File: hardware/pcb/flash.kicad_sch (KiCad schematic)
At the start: 0 parts

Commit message: Update(hardware): Completed some schematics
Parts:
- added C7: 100n, Package_SON:WSON-8-1EP_6x5mm_P1.27mm_EP3.4x4.3mm, symbol Device:C
- added R1: 10k, Package_SON:WSON-8-1EP_6x5mm_P1.27mm_EP3.4x4.3mm, symbol Device:R
- added R2: 10, symbol Device:R
- added U7: IS25WP256D-JLLE, Package_SON:WSON-8-1EP_6x5mm_P1.27mm_EP3.4x4.3mm, symbol IS25WP256D-JLLE:IS25WP256D-JLLE
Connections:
- net CE# (QSPI CSN): now also R1.1
- net HOLD# (IO3): now also U7.7 (HOLD#/RESET#/IO3)
- net SCK: now also R2.1
- net SI (IO0): now also U7.5 (SI/IO0)
- net SO (IO1): now also U7.2 (SO/IO1)
- net WP# (IO2): now also U7.3 (WP#/IO2)
- new net: R1.2, U7.1 (CE#)
- new net: R2.2, U7.6 (SCK)
- new net +1V8: C7.1, U7.8 (VCC)
- new net GNDPWR: C7.2, U7.4 (GND)
- no-connect marks 0 -> 1
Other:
- note added: "Documentation available here"
- note added: "Operation voltage 1.8V (use a level shifter SPI IO)"

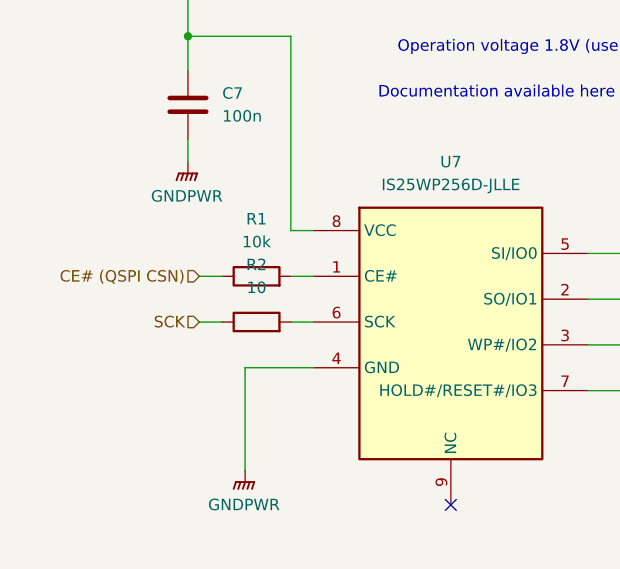
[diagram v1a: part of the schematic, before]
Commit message: Changed GNDPWR to GND and changed GND to speciality GNDs
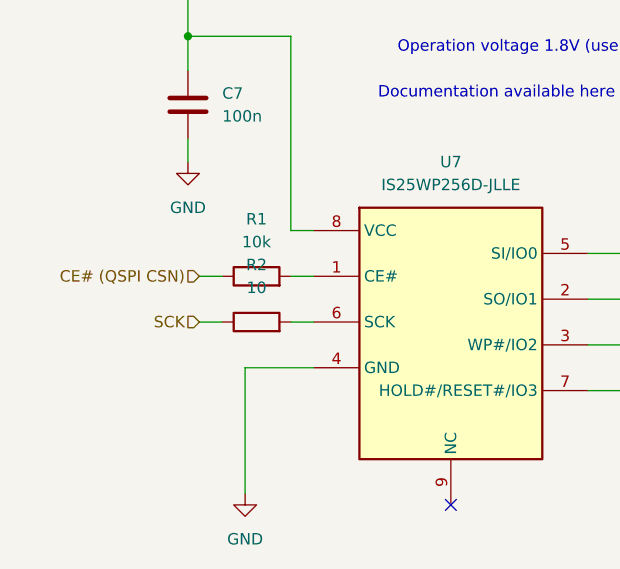
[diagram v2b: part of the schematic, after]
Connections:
- net GNDPWR renamed GND
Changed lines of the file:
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@@
 	(wire
 		(pts
-			(xy 101.6 104.14) (xy 101.6 115.57)
+			(xy 101.6 104.14) (xy 101.6 118.11)
 		)
 		(stroke
@@
 			)
 			(justify right)
-		)
-	)
-	(symbol
-		(lib_id "power:GNDPWR")
-		(at 101.6 115.57 0)
-		(unit 1)
-		(body_style 1)
-		(exclude_from_sim no)
-		(in_bom yes)
-		(on_board yes)
-		(in_pos_files yes)
-		(dnp no)
-		(fields_autoplaced yes)
-		(property "Reference" "#PWR024"
-			(at 101.6 120.65 0)
-			(hide yes)
-			(show_name no)
-			(do_not_autoplace no)
-			(effects
-				(font
-					(size 1.27 1.27)
-				)
-			)
-		)
-		(property "Value" "GNDPWR"
-			(at 101.473 119.38 0)
-			(show_name no)
-			(do_not_autoplace no)
-			(effects
-				(font
-					(size 1.27 1.27)
-				)
-			)
-		)
-		(property "Footprint" ""
-			(at 101.6 116.84 0)
-			(hide yes)
-			(show_name no)
-			(do_not_autoplace no)
-			(effects
-				(font
-					(size 1.27 1.27)
-				)
-			)
-		)
-		(property "Datasheet" ""
-			(at 101.6 116.84 0)
-			(hide yes)
-			(show_name no)
-			(do_not_autoplace no)
-			(effects
-				(font
-					(size 1.27 1.27)
-				)
-			)
-		)
-		(property "Description" "Power symbol creates a global label with name \"GNDPWR\" , global ground"
-			(at 101.6 115.57 0)
-			(hide yes)
-			(show_name no)
-			(do_not_autoplace no)
-			(effects
-				(font
-					(size 1.27 1.27)
-				)
-			)
-		)
-		(pin "1"
-		)
-		(instances
-			(project "test-circuits"
-				(path "/7b1b7b91-6618-446c-b915-39ecd9748633/cf3b1c17-62ba-4998-8a74-365c3fc0ceaf"
-					(reference "#PWR024")
-					(unit 1)
-				)
-			)
-		)
-	)
-	(symbol
-		(lib_id "power:GNDPWR")
-		(at 95.25 81.28 0)
-		(unit 1)
-		(body_style 1)
-		(exclude_from_sim no)
-		(in_bom yes)
-		(on_board yes)
-		(in_pos_files yes)
-		(dnp no)
-		(fields_autoplaced yes)
-		(property "Reference" "#PWR026"
-			(at 95.25 86.36 0)
-			(hide yes)
-			(show_name no)
-			(do_not_autoplace no)
-			(effects
-				(font
-					(size 1.27 1.27)
-				)
-			)
-		)
-		(property "Value" "GNDPWR"
-			(at 95.123 85.09 0)
-			(show_name no)
-			(do_not_autoplace no)
-			(effects
-				(font
-					(size 1.27 1.27)
-				)
-			)
-		)
-		(property "Footprint" ""
-			(at 95.25 82.55 0)
-			(hide yes)
-			(show_name no)
-			(do_not_autoplace no)
-			(effects
-				(font
-					(size 1.27 1.27)
-				)
-			)
-		)
-		(property "Datasheet" ""
-			(at 95.25 82.55 0)
-			(hide yes)
-			(show_name no)
-			(do_not_autoplace no)
-			(effects
-				(font
-					(size 1.27 1.27)
-				)
-			)
-		)
-		(property "Description" "Power symbol creates a global label with name \"GNDPWR\" , global ground"
-			(at 95.25 81.28 0)
-			(hide yes)
-			(show_name no)
-			(do_not_autoplace no)
-			(effects
-				(font
-					(size 1.27 1.27)
-				)
-			)
-		)
-		(pin "1"
-		)
-		(instances
-			(project "test-circuits"
-				(path "/7b1b7b91-6618-446c-b915-39ecd9748633/cf3b1c17-62ba-4998-8a74-365c3fc0ceaf"
-					(reference "#PWR026")
-					(unit 1)
-				)
-			)
 		)
 	)
@@
 	)
 	(symbol
+		(lib_id "power:GND")
+		(at 101.6 118.11 0)
+		(unit 1)
+		(body_style 1)
+		(exclude_from_sim no)
+		(in_bom yes)
+		(on_board yes)
+		(in_pos_files yes)
+		(dnp no)
+		(fields_autoplaced yes)
+		(property "Reference" "#PWR024"
+			(at 101.6 124.46 0)
+			(hide yes)
+			(show_name no)
+			(do_not_autoplace no)
+			(effects
+				(font
+					(size 1.27 1.27)
+				)
+			)
+		)
+		(property "Value" "GND"
+			(at 101.6 123.19 0)
+			(show_name no)
+			(do_not_autoplace no)
+			(effects
+				(font
+					(size 1.27 1.27)
+				)
+			)
+		)
+		(property "Footprint" ""
+			(at 101.6 118.11 0)
+			(hide yes)
+			(show_name no)
+			(do_not_autoplace no)
+			(effects
+				(font
+					(size 1.27 1.27)
+				)
+			)
+		)
+		(property "Datasheet" ""
+			(at 101.6 118.11 0)
+			(hide yes)
+			(show_name no)
+			(do_not_autoplace no)
+			(effects
+				(font
+					(size 1.27 1.27)
+				)
+			)
+		)
+		(property "Description" "Power symbol creates a global label with name \"GND\" , ground"
+			(at 101.6 118.11 0)
+			(hide yes)
+			(show_name no)
+			(do_not_autoplace no)
+			(effects
+				(font
+					(size 1.27 1.27)
+				)
+			)
+		)
+		(pin "1"
+		)
+		(instances
+			(project "test-circuits"
+				(path "/7b1b7b91-6618-446c-b915-39ecd9748633/cf3b1c17-62ba-4998-8a74-365c3fc0ceaf"
+					(reference "#PWR024")
+					(unit 1)
+				)
+			)
+		)
+	)
+	(symbol
 		(lib_id "Device:R")
 		(at 102.87 93.98 90)
@@
 					(unit 1)
 				)
+			)
+		)
+	)
+	(symbol
+		(lib_id "power:GND")
+		(at 95.25 81.28 0)
+		(unit 1)
+		(body_style 1)
+		(exclude_from_sim no)
+		(in_bom yes)
+		(on_board yes)
+		(in_pos_files yes)
+		(dnp no)
+		(fields_autoplaced yes)
+		(property "Reference" "#PWR023"
+			(at 95.25 87.63 0)
+			(hide yes)
+			(show_name no)
+			(do_not_autoplace no)
+			(effects
+				(font
+					(size 1.27 1.27)
+				)
+			)
+		)
+		(property "Value" "GND"
+			(at 95.25 86.36 0)
+			(show_name no)
+			(do_not_autoplace no)
+			(effects
+				(font
+					(size 1.27 1.27)
+				)
+			)
+		)
+		(property "Footprint" ""
+			(at 95.25 81.28 0)
+			(hide yes)
+			(show_name no)
+			(do_not_autoplace no)
+			(effects
+				(font
+					(size 1.27 1.27)
+				)
+			)
+		)
+		(property "Datasheet" ""
+			(at 95.25 81.28 0)
+			(hide yes)
+			(show_name no)
+			(do_not_autoplace no)
+			(effects
+				(font
+					(size 1.27 1.27)
+				)
+			)
+		)
+		(property "Description" "Power symbol creates a global label with name \"GND\" , ground"
+			(at 95.25 81.28 0)
+			(hide yes)
+			(show_name no)
+			(do_not_autoplace no)
+			(effects
+				(font
+					(size 1.27 1.27)
+				)
+			)
+		)
+		(pin "1"
+		)
+		(instances
+			(project "test-circuits"
+				(path "/7b1b7b91-6618-446c-b915-39ecd9748633/cf3b1c17-62ba-4998-8a74-365c3fc0ceaf"
+					(reference "#PWR023")
+					(unit 1)
+				)

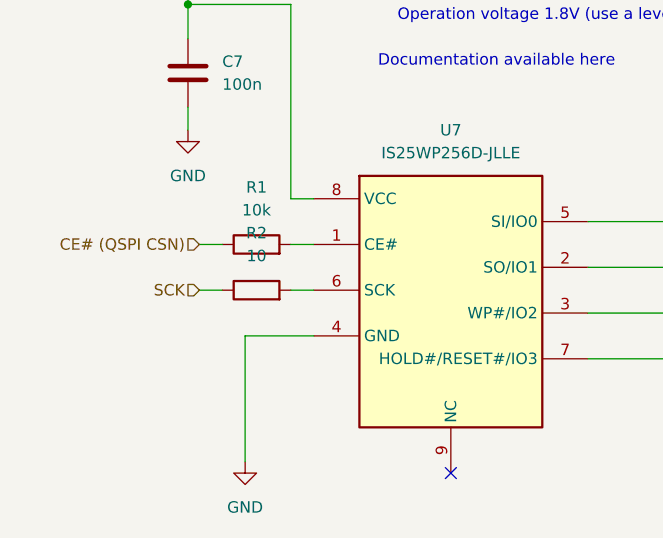
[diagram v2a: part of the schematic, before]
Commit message: Added USB-C to UART connectivity for debugging and flashing
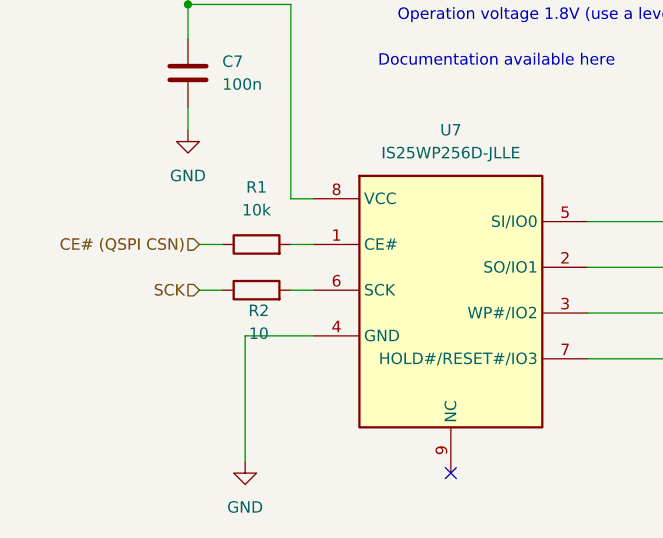
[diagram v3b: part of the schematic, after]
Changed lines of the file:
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@@
 		(in_pos_files yes)
 		(dnp no)
-		(fields_autoplaced yes)
 		(property "Reference" "R2"
-			(at 102.87 92.71 90)
+			(at 103.124 101.346 90)
 			(show_name no)
 			(do_not_autoplace no)
@@
 		)
 		(property "Value" "10"
-			(at 102.87 95.25 90)
+			(at 103.124 103.886 90)
 			(show_name no)
 			(do_not_autoplace no)

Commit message: Update(hardware): Added new flash symbol
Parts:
- removed R2: 10, symbol Device:R
- removed U7: IS25WP256D-JLLE, Package_SON:WSON-8-1EP_6x5mm_P1.27mm_EP3.4x4.3mm, symbol IS25WP256D-JLLE:IS25WP256D-JLLE
- added U7: XT25F128FWOIGT-W, Package_SON:WSON-8-1EP_6x5mm_P1.27mm_EP3.4x4mm, symbol XT25F128F:XT25F128FWOIGT-W
- C7: footprint Package_SON:WSON-8-1EP_6x5mm_P1.27mm_EP3.4x4.3mm -> Package_SO:SOIC-8_3.9x4.9mm_P1.27mm
- R1: footprint Package_SON:WSON-8-1EP_6x5mm_P1.27mm_EP3.4x4.3mm -> (none)
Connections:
- net CE# (QSPI CSN): now also R1.2, U7.1 (CS#); no longer R1.1
- net HOLD# (IO3): now also U7.7 (HOLD#/RESET#/IO3)
- net SCK: now also U7.6 (SCLK)
- net SI (IO0): now also U7.5 (SI/IO0)
- net SO (IO1): now also U7.2 (SO/IO1)
- net WP# (IO2): now also U7.3 (WP#/IO2)
- net +1V8 renamed +3V3
- net +3V3: now also R1.1, U7.8 (VCC)
- net GND renamed GNDPWR
- net GNDPWR: now also U7.4 (VSS)
- no-connect marks 1 -> 0
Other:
- note removed: "Operation voltage 1.8V (use a level shifter SPI IO)"

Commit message: Progress on 3V3 circuit versions.
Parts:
- added U12: XT25F128FWOIGT-W, Package_SON:WSON-8-1EP_6x5mm_P1.27mm_EP3.4x4mm, symbol symbols:XT25F128FWOIGT-W
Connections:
- net +3V3: now also U12.8 (VCC); no longer C7.1, R1.1, U7.8 (VCC)
- net CE# (QSPI CSN): now also U12.1 (CS#); no longer R1.2, U7.1 (CS#)
- net HOLD# (IO3): now also U12.7 (HOLD#/RESET#/IO3)
- net SCK: now also U12.6 (SCLK)
- net SI (IO0): now also U12.5 (SI/IO0)
- net SO (IO1): now also U12.2 (SO/IO1)
- net WP# (IO2): now also U12.3 (WP#/IO2)
- net GNDPWR: no longer names the net of C7.2
- net GNDPWR: no longer U7.4 (VSS)
- new net GND: U12.4 (VSS)

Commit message: Updated broken flash schematic.
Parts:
- removed C7: 100n, Package_SO:SOIC-8_3.9x4.9mm_P1.27mm, symbol Device:C
- removed R1: 10k, symbol Device:R
- removed U12: XT25F128FWOIGT-W, Package_SON:WSON-8-1EP_6x5mm_P1.27mm_EP3.4x4mm, symbol symbols:XT25F128FWOIGT-W
- removed U7: XT25F128FWOIGT-W, Package_SON:WSON-8-1EP_6x5mm_P1.27mm_EP3.4x4mm, symbol XT25F128F:XT25F128FWOIGT-W
- added U7: XT25F128FWOIGT-W, Package_SON:WSON-8-1EP_6x5mm_P1.27mm_EP3.4x4mm, symbol symbols:XT25F128FWOIGT-W
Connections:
- net +3V3: now also U7.8 (VCC)
- net GND: now also U7.4 (VSS)
- new net FLASH CS#: U7.1 (CS#)
- new net FLASH IO0: U7.5 (SI/IO0)
- new net FLASH IO1: U7.2 (SO/IO1)
- new net FLASH IO2: U7.3 (WP#/IO2)
- new net FLASH IO3: U7.7 (HOLD#/RESET#/IO3)
- new net FLASH SCK: U7.6 (SCLK)
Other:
- note removed: "Documentation available here"
